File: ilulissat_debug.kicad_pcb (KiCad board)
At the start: 2 copper layers, 19.4 x 22.6 mm, 3 parts, among them J1 Conn_01x06, J2 Conn_01x04, J3 Conn_01x04

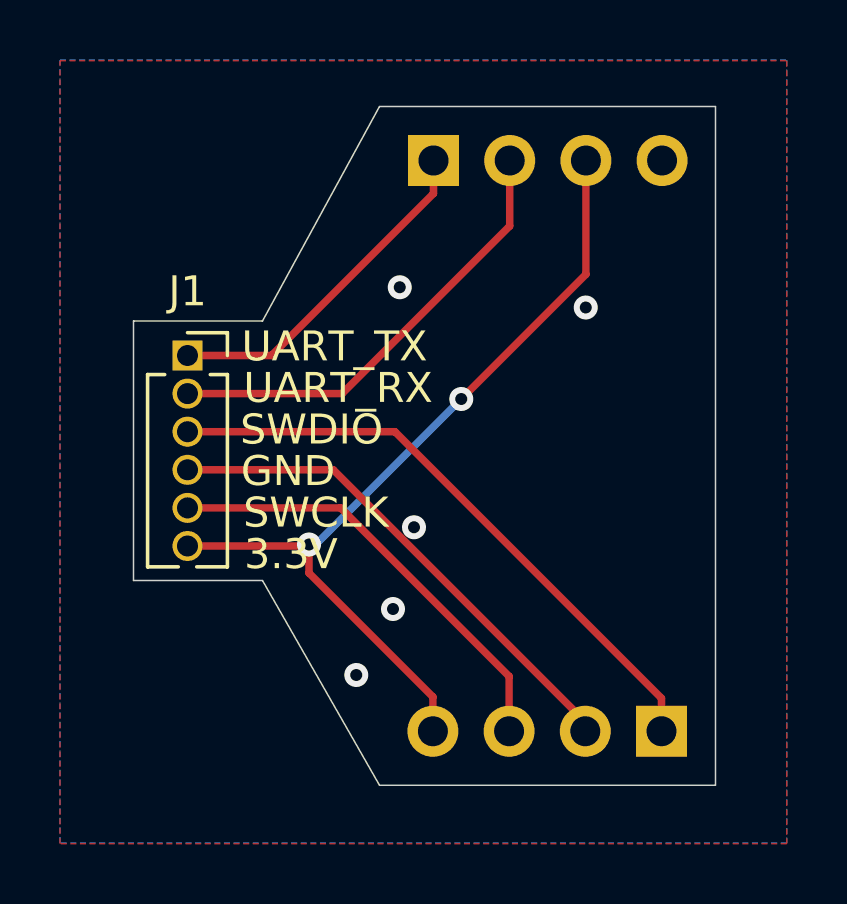
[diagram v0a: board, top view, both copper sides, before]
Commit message: Fix silkscreen and orientation of headers
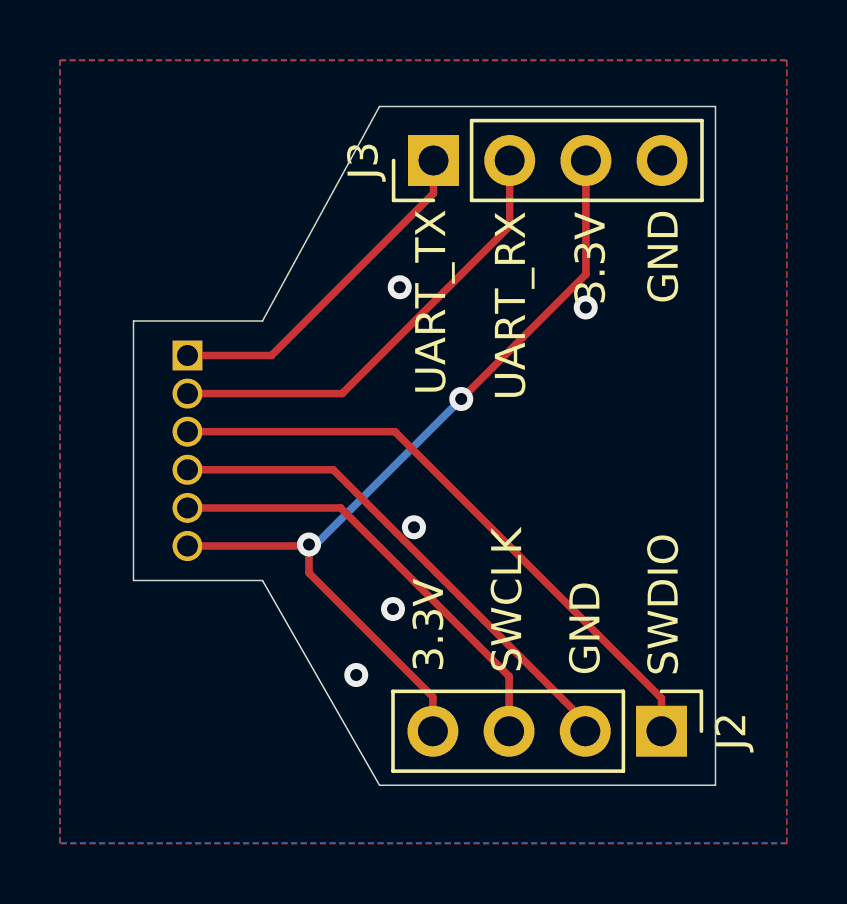
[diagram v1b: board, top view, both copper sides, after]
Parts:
- J1: moved to B.Cu
- J2, J3: moved to F.Cu
- turned J1 to 180 degrees
- turned J2 to 270 degrees
- turned J3 to 90 degrees
